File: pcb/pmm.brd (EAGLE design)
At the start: 30 x 35 mm, 26 parts, among them IC2 REG1117, IC3 STM32F042F4, SW3 324_SW, SW4 324_SW, U2 USBC_16P

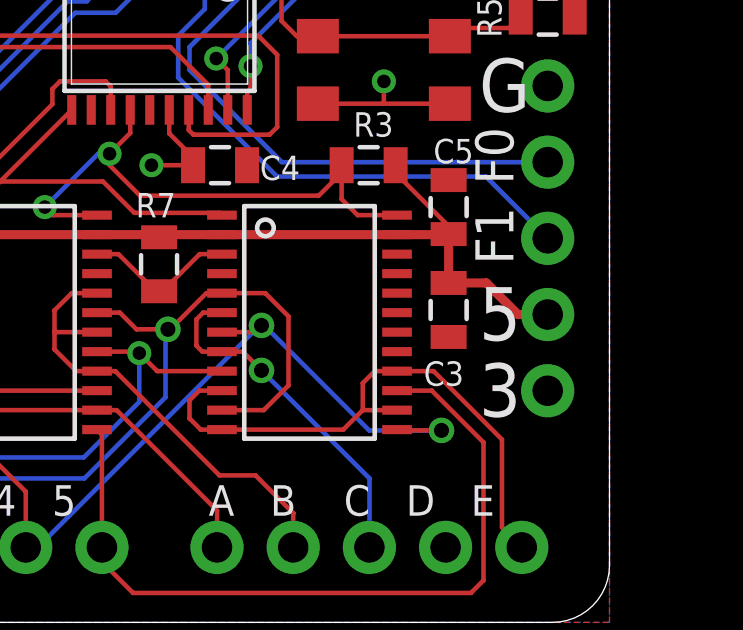
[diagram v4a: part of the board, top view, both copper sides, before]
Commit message: updated bottom layer clearance
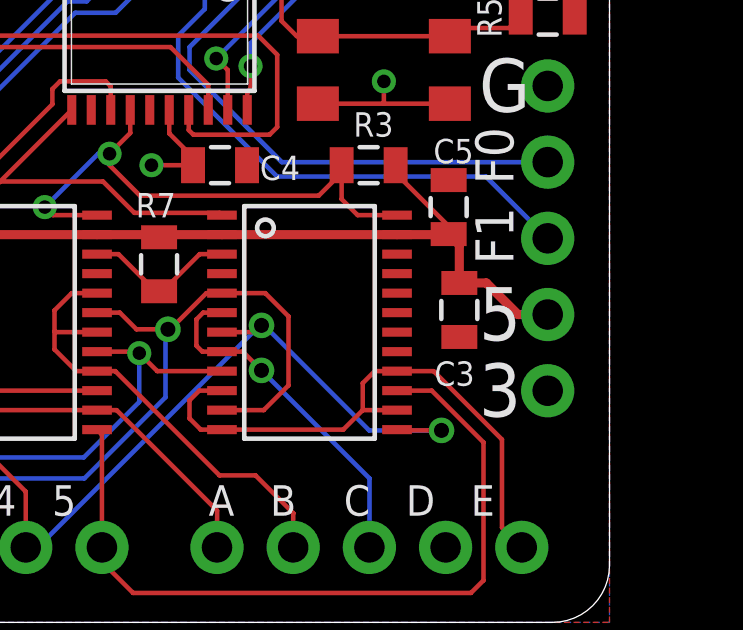
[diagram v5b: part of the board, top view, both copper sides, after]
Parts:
- moved C3 0.36 mm to (25.0, 10.4)
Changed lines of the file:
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@@
 <layer number="37" name="tTest" color="7" fill="1" visible="no" active="yes"/>
 <layer number="38" name="bTest" color="7" fill="1" visible="no" active="yes"/>
-<layer number="39" name="tKeepout" color="4" fill="11" visible="no" active="yes"/>
-<layer number="40" name="bKeepout" color="1" fill="11" visible="no" active="yes"/>
-<layer number="41" name="tRestrict" color="4" fill="10" visible="no" active="yes"/>
-<layer number="42" name="bRestrict" color="1" fill="10" visible="no" active="yes"/>
+<layer number="39" name="tKeepout" color="4" fill="11" visible="yes" active="yes"/>
+<layer number="40" name="bKeepout" color="1" fill="11" visible="yes" active="yes"/>
+<layer number="41" name="tRestrict" color="4" fill="10" visible="yes" active="yes"/>
+<layer number="42" name="bRestrict" color="1" fill="10" visible="yes" active="yes"/>
 <layer number="43" name="vRestrict" color="2" fill="10" visible="no" active="yes"/>
 <layer number="44" name="Drills" color="7" fill="1" visible="no" active="yes"/>
@@
 </element>
 <element name="U$5" library="adafruit_changed" package="1X05" value="PINHD5" x="27.94" y="11.5316" smashed="yes" rot="R270"/>
-<element name="C3" library="clock" package="0805@1" value="10uF" x="24.638" y="10.414" smashed="yes" rot="R90">
-<attribute name="NAME" x="25.146" y="8.6995" size="0.8128" layer="25" rot="R180"/>
+<element name="C3" library="clock" package="0805@1" value="10uF" x="24.9936" y="10.414" smashed="yes" rot="R90">
+<attribute name="NAME" x="25.5016" y="8.6995" size="0.8128" layer="25" rot="R180"/>
 </element>
 <element name="C5" library="clock" package="0805@1" value="10uF" x="24.638" y="13.843" smashed="yes" rot="R270">
@@
 <contactref element="IC2" pad="4"/>
 <contactref element="C2" pad="1"/>
-<polygon width="0.1524" layer="16">
+<polygon width="0.1524" layer="16" isolate="0.254">
 <vertex x="0" y="35"/>
 <vertex x="30" y="35"/>
@@
 <wire x1="27.94" y1="10.2616" x2="26.9494" y2="10.2616" width="0.3048" layer="1"/>
 <wire x1="26.9494" y1="10.2616" x2="25.897" y2="11.314" width="0.3048" layer="1"/>
-<wire x1="25.897" y1="11.314" x2="24.638" y2="11.314" width="0.3048" layer="1"/>
-<wire x1="24.638" y1="11.314" x2="24.638" y2="12.943" width="0.3048" layer="1"/>
+<wire x1="25.897" y1="11.314" x2="24.9936" y2="11.314" width="0.3048" layer="1"/>
+<wire x1="24.9936" y1="12.5874" x2="24.9936" y2="11.314" width="0.3048" layer="1"/>
+<wire x1="24.9936" y1="12.5874" x2="24.638" y2="12.943" width="0.3048" layer="1"/>
 <wire x1="22.9178" y1="12.925" x2="24.62" y2="12.925" width="0.3048" layer="1"/>
 <wire x1="24.62" y1="12.925" x2="24.638" y2="12.943" width="0.3048" layer="1"/>
